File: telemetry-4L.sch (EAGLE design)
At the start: 73 parts, among them SW1 MF-SW-TACT-4.2MM, SW2 PCM12SMTR, U1 ATSAMD21G18A-MUT, U2 SPX3819M5-L-3-0, U3 MCP73831T-2ACI/OT, U4 IRLML6344TRPBF, U5 SIM868, U6 BMP280, U7 MPU-9250, U8 TPS61253YFFR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

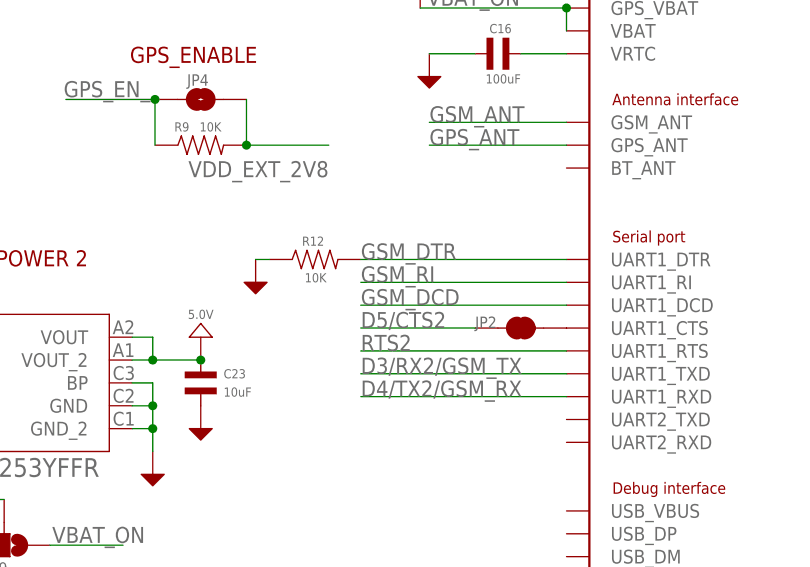
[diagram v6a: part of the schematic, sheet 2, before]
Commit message: Added connection to DCD shared with SWCLK  - might be needed for FTP and similar
Try using FTP and if not needed, kill this again
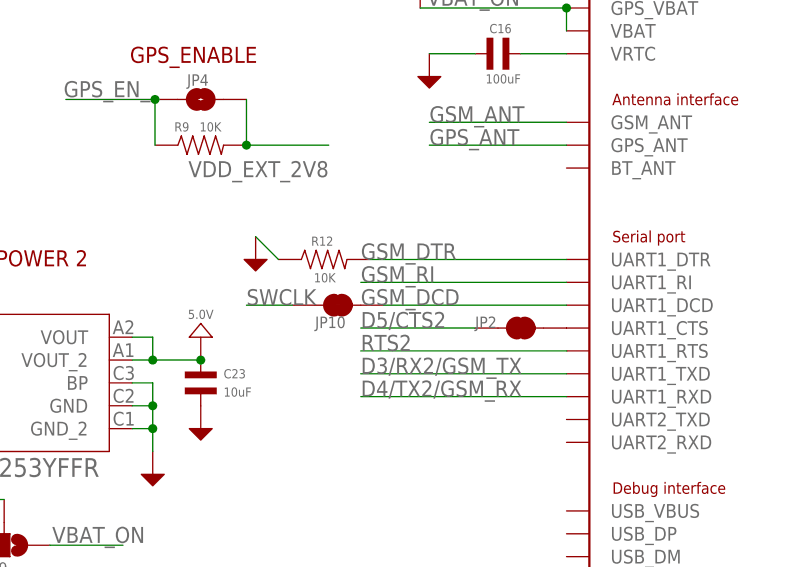
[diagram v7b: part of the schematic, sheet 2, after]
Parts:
- added JP10: JUMPER-PAD-2-NC_BY_TRACE, SparkFun-Passives:JUMPER-PAD-2-NC_BY_TRACE
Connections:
- net D0/RX0/CTS2 renamed D0/RX0
- net GSM_DCD: now also JP10.2
- net SWCLK: now also JP10.1
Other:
- moved on the sheet: R12
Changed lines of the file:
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@@
 <part name="U$37" library="MF_Aesthetics" deviceset="GND_RAIL" device=""/>
 <part name="U$61" library="MF_Aesthetics" deviceset="GND_RAIL" device=""/>
+<part name="JP10" library="SparkFun-Passives" deviceset="JUMPER-PAD-2-NC_BY_TRACE" device="">
+<attribute name="POPULATE" value="0"/>
+</part>
 </parts>
 <sheets>
@@
 </segment>
 </net>
-<net name="D0/RX0/CTS2" class="0">
+<net name="D0/RX0" class="0">
 <segment>
 <wire x1="121.92" y1="66.04" x2="104.14" y2="66.04" width="0.1524" layer="91"/>
@@
 <attribute name="VALUE" x="96.012" y="141.478" size="1.016" layer="96" font="vector" rot="R90"/>
 </instance>
-<instance part="R12" gate="G$1" x="137.16" y="121.92" smashed="yes" rot="R90">
-<attribute name="NAME" x="138.176" y="123.444" size="1.016" layer="95" font="vector" rot="R180" align="top-left"/>
-<attribute name="VALUE" x="138.43" y="120.396" size="1.016" layer="96" font="vector" rot="R180"/>
-</instance>
-<instance part="U$37" gate="G$1" x="130.556" y="119.38"/>
+<instance part="R12" gate="G$1" x="138.176" y="121.92" smashed="yes" rot="R90">
+<attribute name="NAME" x="139.192" y="123.444" size="1.016" layer="95" font="vector" rot="R180" align="top-left"/>
+<attribute name="VALUE" x="139.446" y="120.396" size="1.016" layer="96" font="vector" rot="R180"/>
+</instance>
+<instance part="U$37" gate="G$1" x="130.556" y="121.92"/>
 <instance part="U$61" gate="G$1" x="149.86" y="142.24"/>
+<instance part="JP10" gate="G$1" x="139.7" y="116.84" smashed="yes">
+<attribute name="NAME" x="137.16" y="114.3" size="1.27" layer="95"/>
+<attribute name="POPULATE" x="139.7" y="116.84" size="1.778" layer="96" display="off"/>
+</instance>
 </instances>
 <busses>
@@
 <segment>
 <pinref part="R12" gate="G$1" pin="P$1"/>
-<wire x1="130.556" y1="121.92" x2="132.08" y2="121.92" width="0.1524" layer="91"/>
+<wire x1="130.556" y1="124.46" x2="133.096" y2="121.92" width="0.1524" layer="91"/>
 <pinref part="U$37" gate="G$1" pin="P$1"/>
 </segment>
@@
 <segment>
 <pinref part="U5" gate="G$1" pin="UART1_DCD"/>
-<wire x1="165.1" y1="116.84" x2="142.24" y2="116.84" width="0.1524" layer="91"/>
+<wire x1="165.1" y1="116.84" x2="144.78" y2="116.84" width="0.1524" layer="91"/>
 <label x="142.24" y="116.84" size="1.778" layer="95"/>
+<pinref part="JP10" gate="G$1" pin="2"/>
 </segment>
 </net>
@@
 <segment>
 <pinref part="U5" gate="G$1" pin="UART1_DTR"/>
-<wire x1="142.24" y1="121.92" x2="165.1" y2="121.92" width="0.1524" layer="91"/>
+<wire x1="143.256" y1="121.92" x2="165.1" y2="121.92" width="0.1524" layer="91"/>
 <label x="142.24" y="121.92" size="1.778" layer="95"/>
 <pinref part="R12" gate="G$1" pin="P$2"/>
@@
 </segment>
 </net>
+<net name="SWCLK" class="0">
+<segment>
+<pinref part="JP10" gate="G$1" pin="1"/>
+<wire x1="134.62" y1="116.84" x2="129.54" y2="116.84" width="0.1524" layer="91"/>
+<label x="129.54" y="116.84" size="1.778" layer="95"/>
+</segment>
+</net>

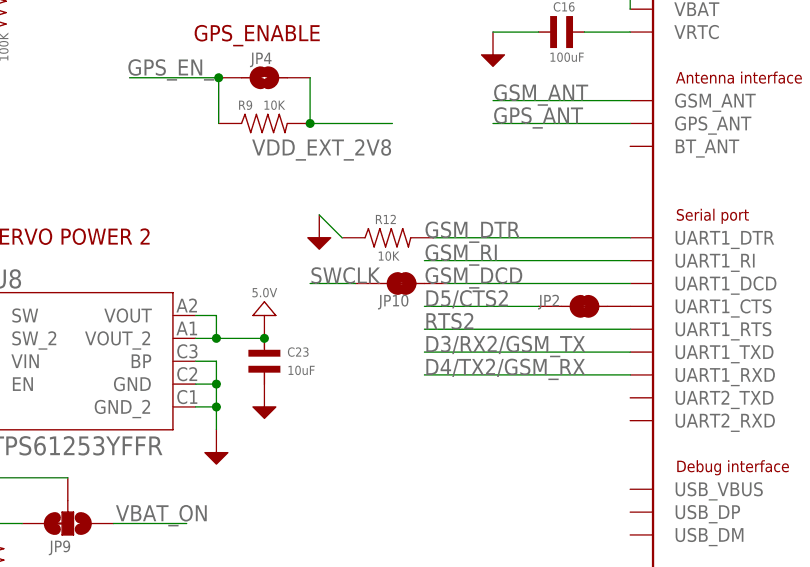
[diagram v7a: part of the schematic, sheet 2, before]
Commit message: Fixed the PCB to reflect last change in schematic
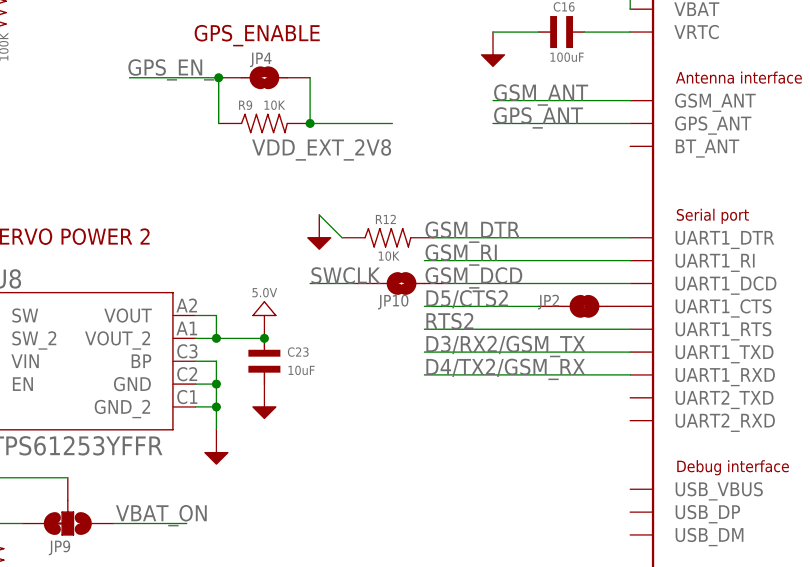
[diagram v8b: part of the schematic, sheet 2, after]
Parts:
- JP10: value JUMPER-PAD-2-NC_BY_TRACE -> JUMPER-PAD-2-NOYES_SILK; device SparkFun-Passives:JUMPER-PAD-2-NC_BY_TRACE -> SparkFun-Passives:JUMPER-PAD-2-NOYES_SILK
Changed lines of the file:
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@@
 <part name="U$37" library="MF_Aesthetics" deviceset="GND_RAIL" device=""/>
 <part name="U$61" library="MF_Aesthetics" deviceset="GND_RAIL" device=""/>
-<part name="JP10" library="SparkFun-Passives" deviceset="JUMPER-PAD-2-NC_BY_TRACE" device="">
+<part name="JP10" library="SparkFun-Passives" deviceset="JUMPER-PAD-2-NO" device="YES_SILK">
 <attribute name="POPULATE" value="0"/>
 </part>
